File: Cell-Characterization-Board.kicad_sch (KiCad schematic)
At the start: 6 parts, among them IC2 INA4180A2IPWR, IC5 MCP3304-CI_SL, SW1 SW_Push, U1 ESP32-S3-WROOM-1

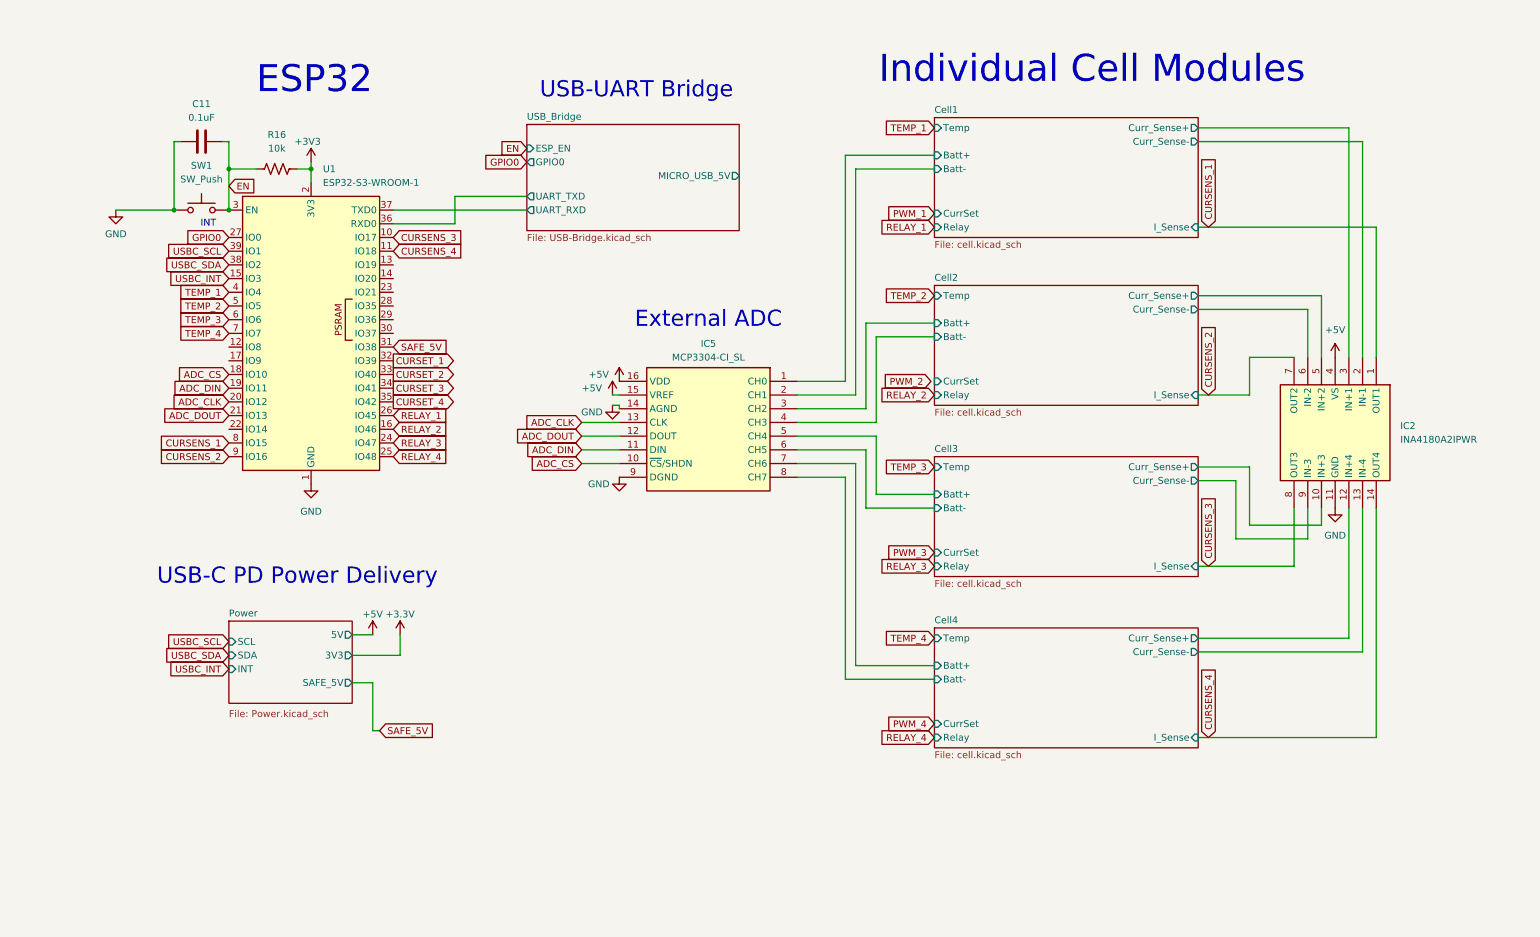
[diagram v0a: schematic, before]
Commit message: added logic level translator
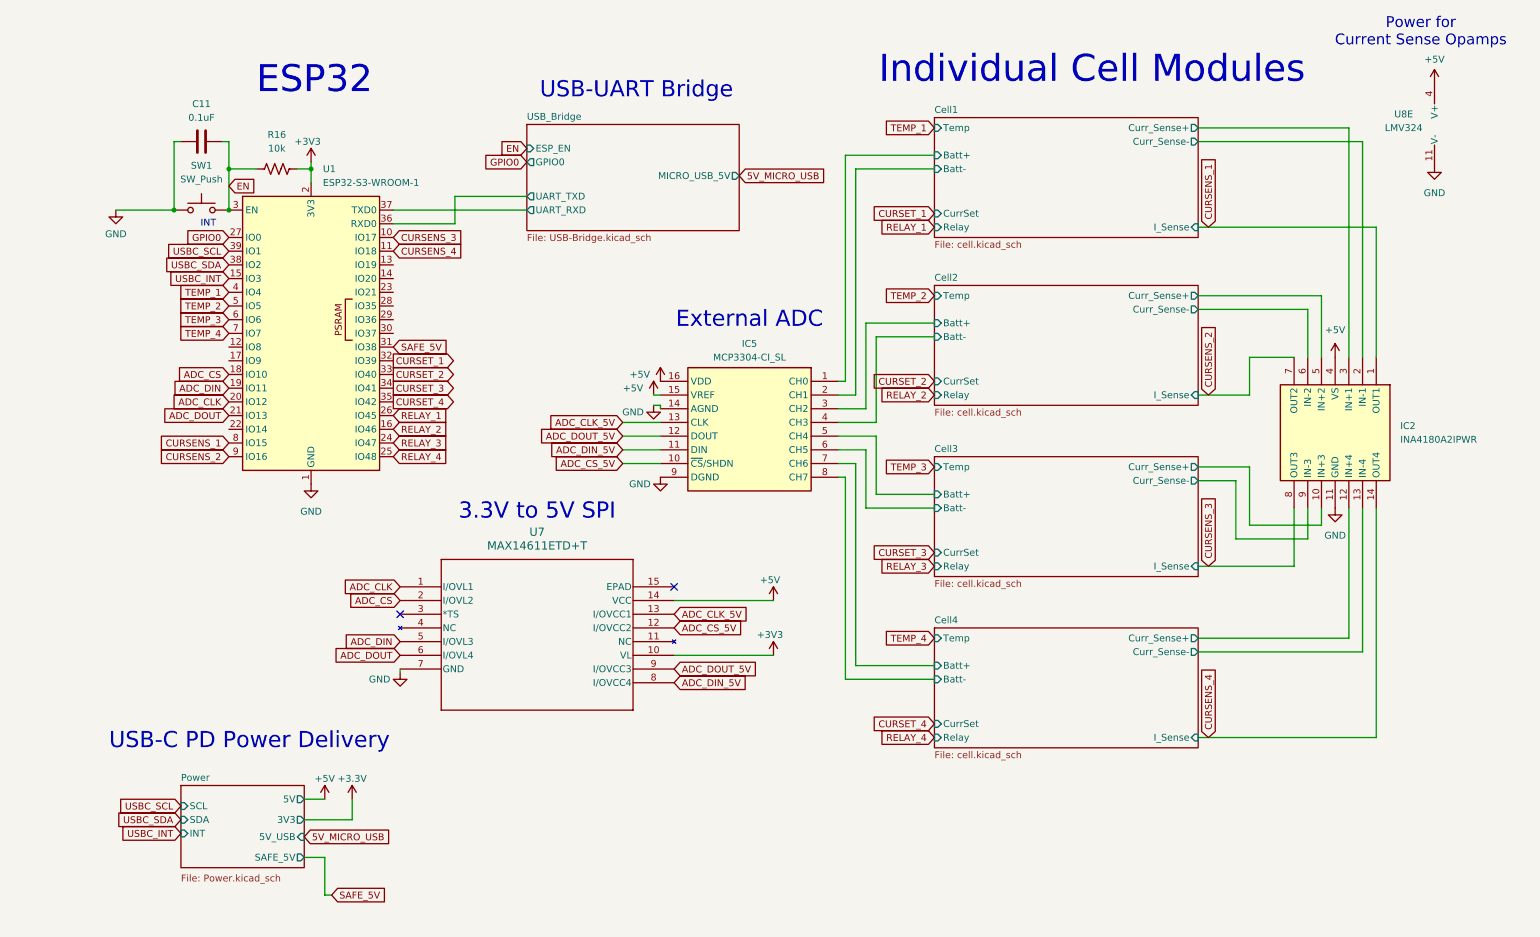
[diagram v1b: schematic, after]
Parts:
- added U7: MAX14611ETD+T, 21-0137_T1433+2C_MXM, symbol 2025-02-22_18-32-49:MAX14611ETD+T
- added U8: LMV324, symbol Amplifier_Operational:LMV324
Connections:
- net +3V3: now also U7.10 (VL)
- net +5V: now also U7.14 (VCC), U8.4 (V+)
- net ADC_CLK: now also U7.1 (I/OVL1); no longer IC5.13 (CLK)
- net ADC_CS: now also U7.2 (I/OVL2); no longer IC5.10 (~{CS}/SHDN)
- net ADC_DIN: now also U7.5 (I/OVL3); no longer IC5.11 (DIN)
- net ADC_DOUT: now also U7.6 (I/OVL4); no longer IC5.12 (DOUT)
- net GND: now also U7.7 (GND), U8.11 (V-)
- new net ADC_CLK_5V: IC5.13 (CLK), U7.13 (I/OVCC1)
- new net ADC_CS_5V: IC5.10 (~{CS}/SHDN), U7.12 (I/OVCC2)
- new net ADC_DIN_5V: IC5.11 (DIN), U7.8 (I/OVCC4)
- new net ADC_DOUT_5V: IC5.12 (DOUT), U7.9 (I/OVCC3)
- no-connect marks 0 -> 2
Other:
- sheet Power ports: added 5V_USB; removed none
- note added: "3.3V to 5V SPI"
- note added: "Power for Current Sense Opamps"
- moved on the sheet: IC5

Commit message: added screen and gpio buttons
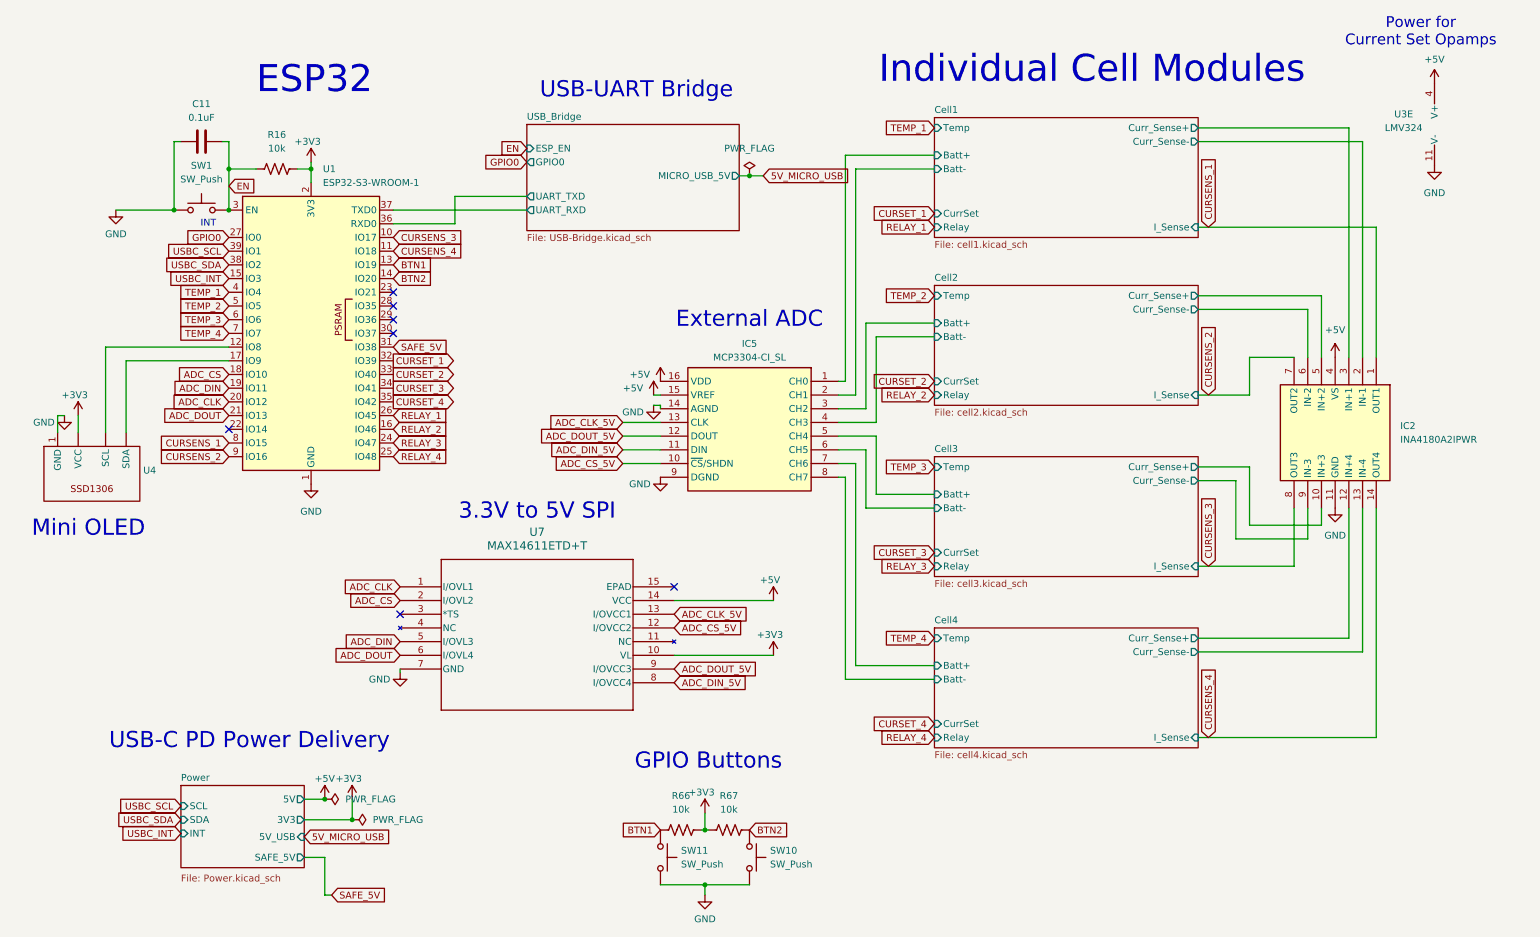
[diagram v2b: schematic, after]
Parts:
- added R66, R67: 10k, symbol Device:R_US
- added SW10, SW11: SW_Push, symbol Switch:SW_Push
- added U4: ~, symbol SSD1306:SSD1306
- renumbered U8 to U3
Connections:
- net +3V3: now also R66.2, R67.1, U4. (VCC)
- net GND: now also SW10.2, SW11.2, U4.1 (GND)
- net at U1.12 (IO8): now also U4. (VCC)
- net BTN1: now reaches U1.13 (IO19)
- net BTN1: now also R66.1, SW11.1
- net BTN2: now reaches U1.14 (IO20)
- net BTN2: now also R67.2, SW10.1
- net at U1.17 (IO9): now also U4. (VCC)
- no-connect marks 2 -> 7
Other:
- sheet Cell1: file cell.kicad_sch -> cell1.kicad_sch
- sheet Cell2: file cell.kicad_sch -> cell2.kicad_sch
- sheet Cell3: file cell.kicad_sch -> cell3.kicad_sch
- sheet Cell4: file cell.kicad_sch -> cell4.kicad_sch
- note added: "GPIO Buttons"
- note added: "Mini OLED"
- note added: "Power for Current Set Opamps"
- note removed: "Power for Current Sense Opamps"

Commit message: Updated current control loop hardware
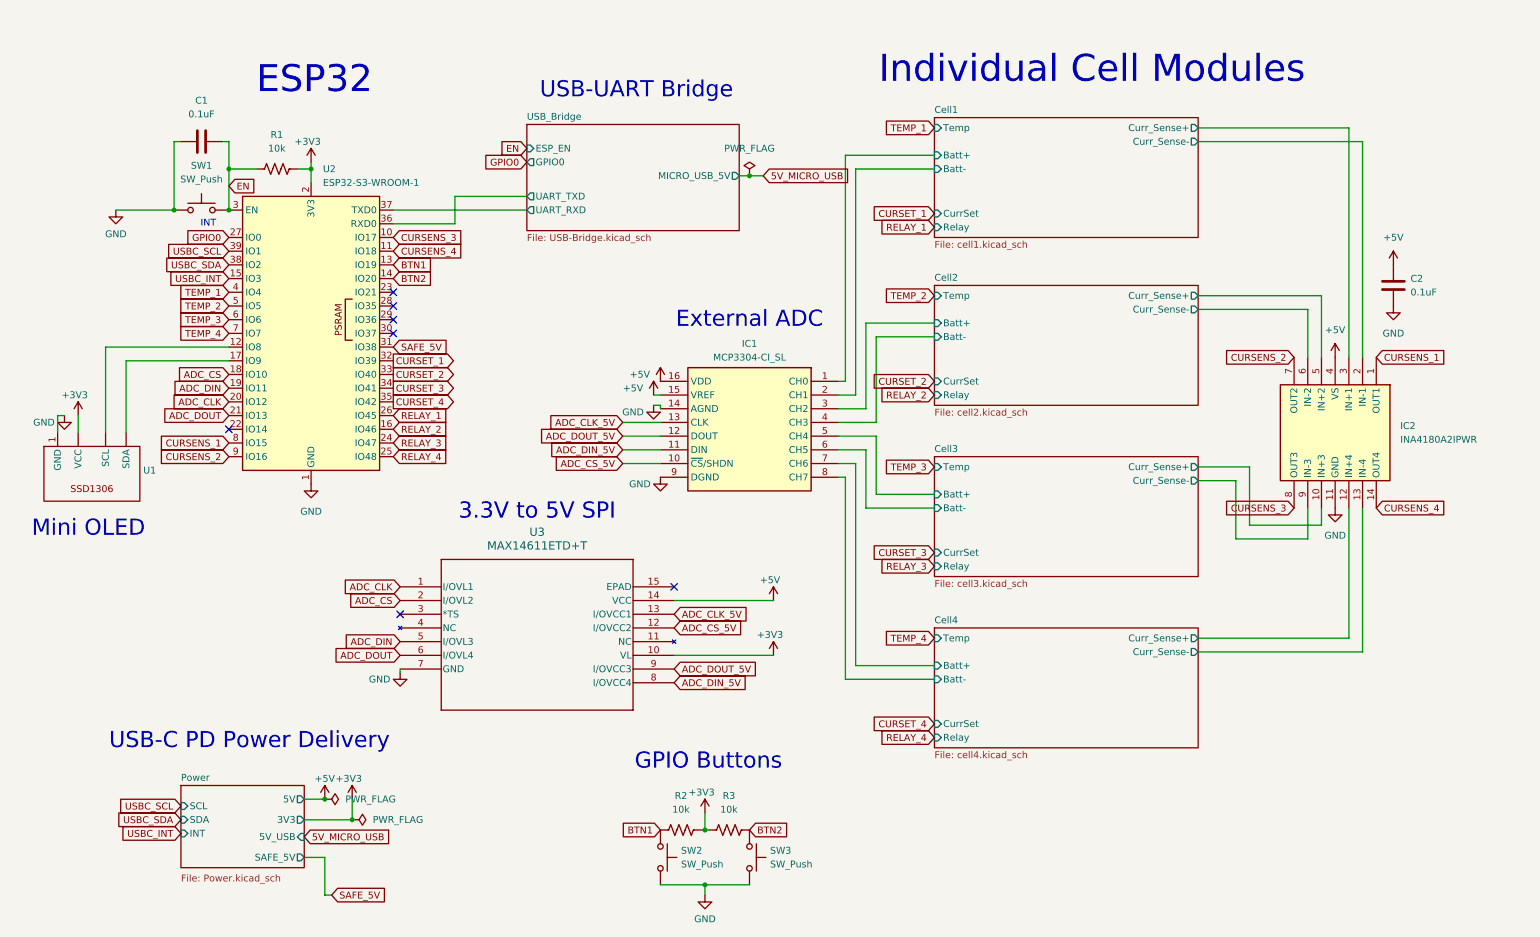
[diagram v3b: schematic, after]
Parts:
- removed C11: 0.1uF, symbol Device:C
- removed U3: LMV324, symbol Amplifier_Operational:LMV324
- added C1, C2: 0.1uF, symbol Device:C
- renumbered IC5 to IC1, R16 to R1, R66 to R2, R67 to R3, SW11 to SW2, SW10 to SW3, U4 to U1, U1 to U2, U7 to U3
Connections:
- net +5V: now also C2.1
- net EN: now also C1.2
- net GND: now also C1.1, C2.2
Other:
- sheet Cell1 ports: added none; removed I_Sense
- sheet Cell2 ports: added none; removed I_Sense
- sheet Cell3 ports: added none; removed I_Sense
- sheet Cell4 ports: added none; removed I_Sense
- note removed: "Power for Current Set Opamps"

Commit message: added battery holder footprint
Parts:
- C1, C2: footprint (none) -> Capacitor_SMD:C_0805_2012Metric
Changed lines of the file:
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@@
 			)
 		)
-		(property "Footprint" ""
+		(property "Footprint" "Capacitor_SMD:C_0805_2012Metric"
 			(at 266.3952 74.93 0)
 			(effects
@@
 			)
 		)
-		(property "Footprint" ""
+		(property "Footprint" "Capacitor_SMD:C_0805_2012Metric"
 			(at 48.26 43.4848 0)
 			(effects

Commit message: footprints and components for buck and power
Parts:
- R1, R2, R3: footprint (none) -> Resistor_SMD:R_0805_2012Metric
- SW1, SW2, SW3: footprint (none) -> ExternalFootprints:SW_1825910-6-4
- U1: footprint (none) -> ExternalFootprints:128x64OLED
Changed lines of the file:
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@@
 			)
 		)
-		(property "Footprint" ""
+		(property "Footprint" "Resistor_SMD:R_0805_2012Metric"
 			(at 133.604 171.069 90)
 			(effects
@@
 			)
 		)
-		(property "Footprint" ""
+		(property "Footprint" "Resistor_SMD:R_0805_2012Metric"
 			(at 58.674 48.514 90)
 			(effects
@@
 			)
 		)
-		(property "Footprint" ""
+		(property "Footprint" "Resistor_SMD:R_0805_2012Metric"
 			(at 142.494 171.069 90)
 			(effects
@@
 			)
 		)
-		(property "Footprint" ""
+		(property "Footprint" "ExternalFootprints:SW_1825910-6-4"
 			(at 44.45 52.07 0)
 			(effects
@@
 			)
 		)
-		(property "Footprint" ""
+		(property "Footprint" "ExternalFootprints:128x64OLED"
 			(at 24.13 107.315 0)
 			(effects
@@
 			)
 		)
-		(property "Footprint" ""
+		(property "Footprint" "ExternalFootprints:SW_1825910-6-4"
 			(at 151.13 177.165 0)
 			(effects
@@
 			)
 		)
-		(property "Footprint" ""
+		(property "Footprint" "ExternalFootprints:SW_1825910-6-4"
 			(at 134.62 177.165 0)
 			(effects

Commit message: updated symbol for screen and added testpoints
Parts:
- added TP19: uUSB_VOUT, UTSVT_Special:TestPoint_HEX_3mmID, symbol Connector:TestPoint
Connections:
- net +3V3: now also U1.2 (VCC); no longer U1. (VCC)
- net 5V_MICRO_USB: now also TP19.1
- net at U2.12 (IO8): now also U1.3 (SCL); no longer U1. (VCC)
- net at U2.17 (IO9): now also U1.4 (SDA); no longer U1. (VCC)
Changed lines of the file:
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@@
 	)
 	(junction
-		(at 72.39 170.18)
+		(at 74.93 170.18)
 		(diameter 0)
 		(color 0 0 0 0)
@@
 	(wire
 		(pts
-			(xy 72.39 166.37) (xy 72.39 170.18)
+			(xy 74.93 166.37) (xy 74.93 170.18)
 		)
 		(stroke
@@
 	(wire
 		(pts
-			(xy 63.5 170.18) (xy 72.39 170.18)
+			(xy 63.5 170.18) (xy 74.93 170.18)
 		)
 		(stroke
@@
 	(wire
 		(pts
-			(xy 148.59 50.8) (xy 146.05 50.8)
-		)
-		(stroke
-			(width 0)
-			(type default)
-		)
-	)
-	(wire
-		(pts
 			(xy 122.555 101.6) (xy 129.54 101.6)
 		)
@@
 	(wire
 		(pts
+			(xy 75.565 170.18) (xy 74.93 170.18)
+		)
+		(stroke
+			(width 0)
+			(type default)
+		)
+	)
+	(wire
+		(pts
 			(xy 49.53 44.45) (xy 49.53 49.53)
 		)
@@
 	(wire
 		(pts
+			(xy 146.05 50.8) (xy 148.59 50.8)
+		)
+		(stroke
+			(width 0)
+			(type default)
+		)
+	)
+	(wire
+		(pts
 			(xy 49.53 57.15) (xy 49.53 49.53)
 		)
@@
 		(on_board yes)
 		(dnp no)
-		(fields_autoplaced yes)
 		(property "Reference" "#FLG01"
 			(at 69.215 166.37 0)
@@
 		)
 		(property "Value" "PWR_FLAG"
-			(at 71.12 166.3699 90)
+			(at 64.77 168.91 90)
 			(effects
 				(font
@@
 	(symbol
 		(lib_id "power:PWR_FLAG")
-		(at 72.39 170.18 270)
+		(at 75.565 170.18 270)
 		(unit 1)
 		(exclude_from_sim no)
@@
 		(fields_autoplaced yes)
 		(property "Reference" "#FLG02"
-			(at 74.295 170.18 0)
+			(at 77.47 170.18 0)
 			(effects
 				(font
@@
 		)
 		(property "Value" "PWR_FLAG"
-			(at 76.2 170.1799 90)
+			(at 79.375 170.1799 90)
 			(effects
 				(font
@@
 		)
 		(property "Footprint" ""
-			(at 72.39 170.18 0)
+			(at 75.565 170.18 0)
 			(effects
 				(font
@@
 		)
 		(property "Datasheet" "~"
-			(at 72.39 170.18 0)
+			(at 75.565 170.18 0)
 			(effects
 				(font
@@
 		)
 		(property "Description" "Special symbol for telling ERC where power comes from"
-			(at 72.39 170.18 0)
+			(at 75.565 170.18 0)
 			(effects
 				(font
@@
 			)
 		)
-		(pin ""
+		(pin "3"
 		)
-		(pin ""
+		(pin "4"
 		)
-		(pin ""
+		(pin "2"
 		)
 		(pin "1"
@@
 	(symbol
 		(lib_id "power:+3V3")
-		(at 72.39 166.37 0)
+		(at 74.93 166.37 0)
 		(unit 1)
 		(exclude_from_sim no)
@@
 		(dnp no)
 		(property "Reference" "#PWR07"
-			(at 72.39 170.18 0)
+			(at 74.93 170.18 0)
 			(effects
 				(font
@@
 		)
 		(property "Value" "+3V3"
-			(at 71.755 162.56 0)
+			(at 74.295 162.56 0)
 			(effects
 				(font
@@
 		)
 		(property "Footprint" ""
-			(at 72.39 166.37 0)
+			(at 74.93 166.37 0)
 			(effects
 				(font
@@
 		)
 		(property "Datasheet" ""
-			(at 72.39 166.37 0)
+			(at 74.93 166.37 0)
 			(effects
 				(font
@@
 		)
 		(property "Description" "Power symbol creates a global label with name \"+3V3\""
-			(at 72.39 166.37 0)
+			(at 74.93 166.37 0)
 			(effects
 				(font
@@
 					(unit 1)
 				)
+			)
+		)
+	)
+	(symbol
+		(lib_id "Connector:TestPoint")
+		(at 146.05 50.8 180)
+		(unit 1)
+		(exclude_from_sim no)
+		(in_bom yes)
+		(on_board yes)
+		(dnp no)
+		(property "Reference" "TP19"
+			(at 147.32 53.975 0)
+			(effects
+				(font
+					(size 1.27 1.27)
+				)
+				(justify right)
+			)
+		)
+		(property "Value" "uUSB_VOUT"
+			(at 147.32 56.515 0)
+			(effects
+				(font
+					(size 1.27 1.27)
+				)
+				(justify right)
+			)
+		)
+		(property "Footprint" "UTSVT_Special:TestPoint_HEX_3mmID"
+			(at 140.97 50.8 0)
+			(effects
+				(font
+					(size 1.27 1.27)
+				)
+				(hide yes)
+			)
+		)
+		(property "Datasheet" "~"
+			(at 140.97 50.8 0)
+			(effects
+				(font
+					(size 1.27 1.27)
+				)
+				(hide yes)
+			)
+		)
+		(property "Description" "test point"
+			(at 146.05 50.8 0)
+			(effects
+				(font
+					(size 1.27 1.27)
+				)
+				(hide yes)
+			)
+		)
+		(pin "1"
+		)
+		(instances
+			(project "Cell-Characterization-Board"
+				(path "/8cf78a1b-eb7a-4166-aa75-ad898a030304"
+					(reference "TP19")
+					(unit 1)
+				)
